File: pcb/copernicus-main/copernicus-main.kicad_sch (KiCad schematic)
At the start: 77 parts, among them J10 FAN_1, J11 FAN_2, J2 USB_C_14P, J3 BATT_IN, J4 CH_IN, J5 M1_PWR, J6 M2_PWR, J7 OUT_1, J8 OUT_2, J9 OUT_3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

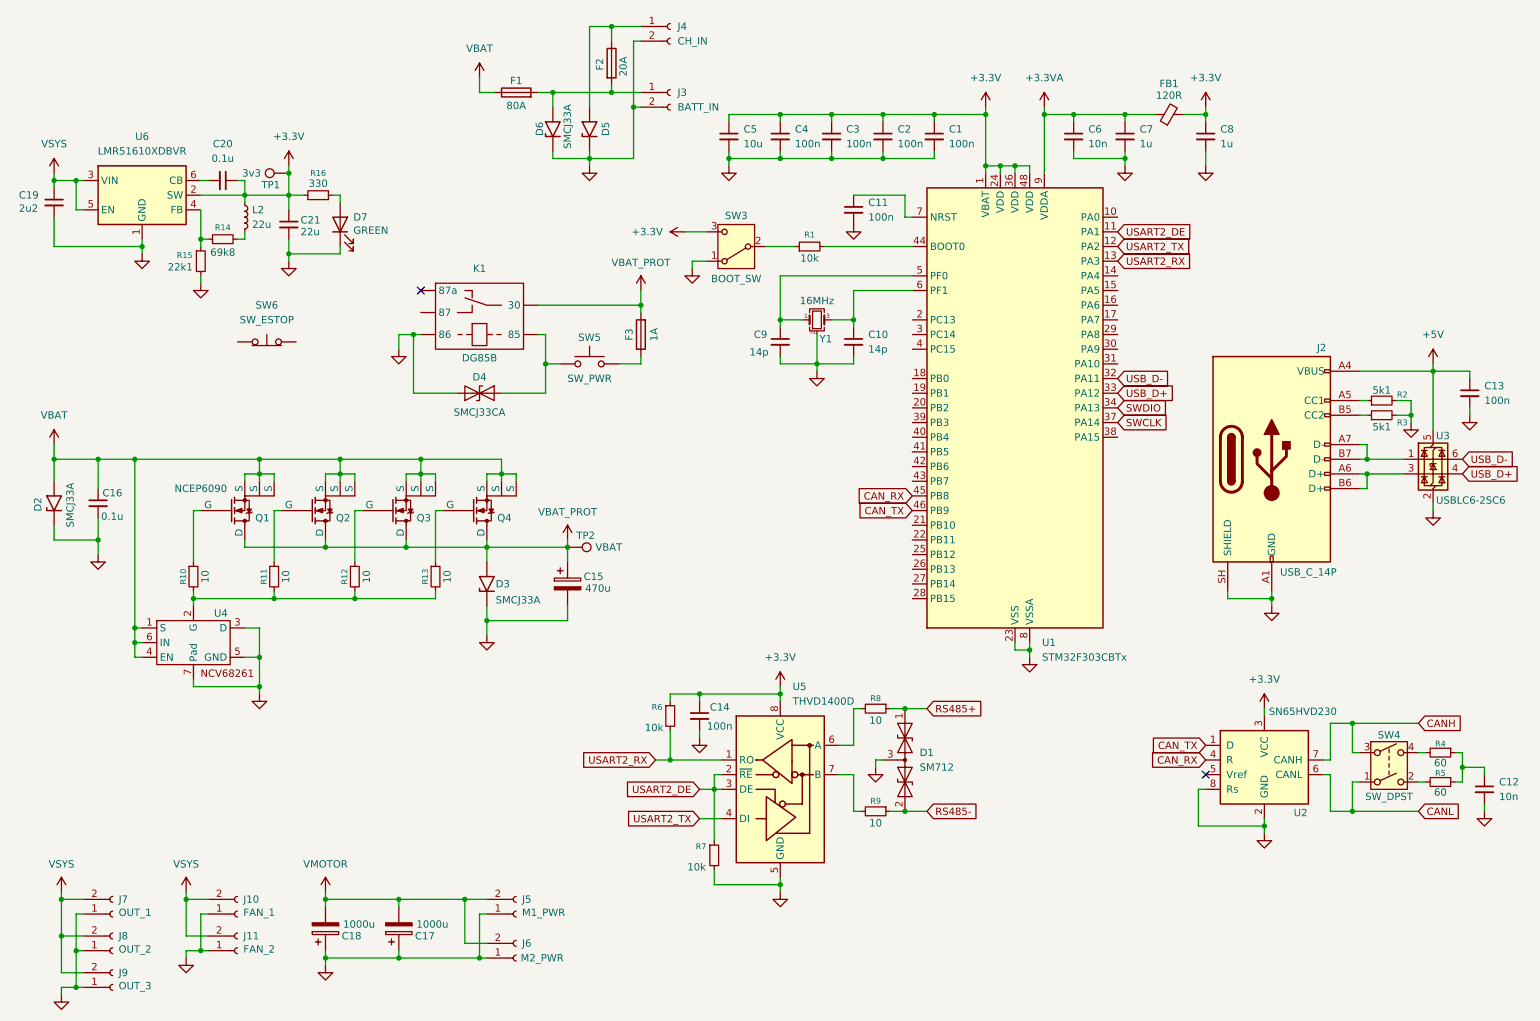
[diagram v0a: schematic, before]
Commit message: docs(pcb): added estop & mcu motor power control
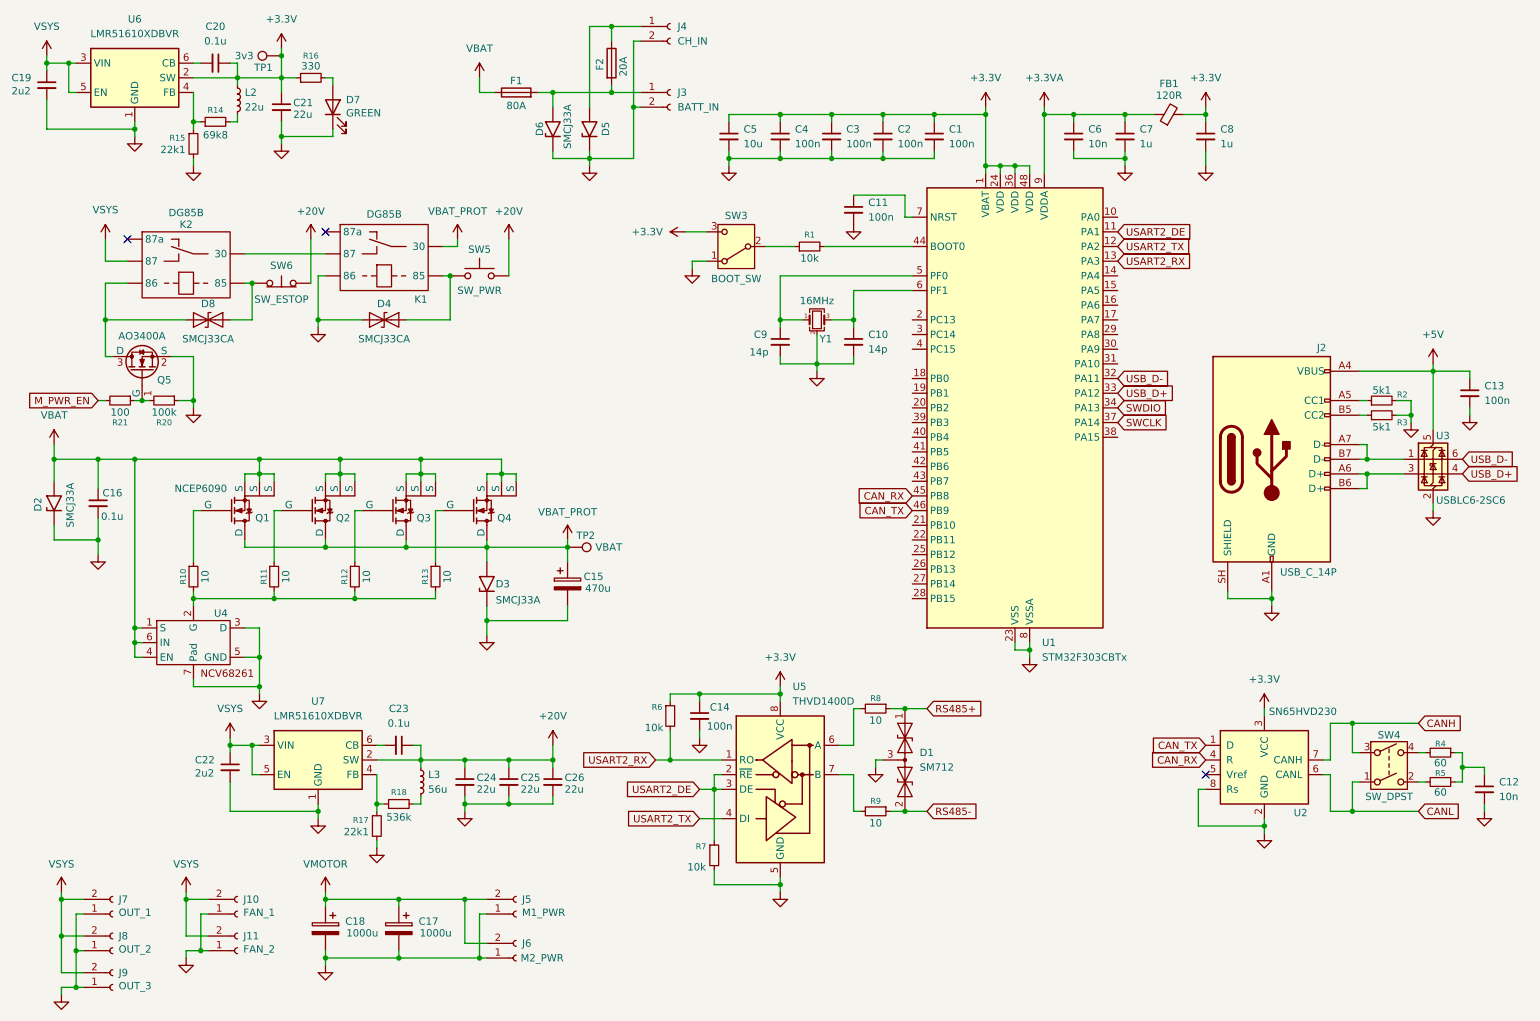
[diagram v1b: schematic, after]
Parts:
- removed F3: 1A, symbol Device:Fuse
- added C22: 2u2, symbol Device:C_Small
- added C23: 0.1u, symbol Device:C_Small
- added C24, C25, C26: 22u, symbol Device:C_Small
- added D8: SMCJ33CA, Diode_SMD:D_SOD-323, symbol component-addon:SMCJ33CA
- added K2: DG85B, symbol component-addon:DG85B
- added L3: 56u, symbol Device:L_Small
- added Q5: AO3400A, Package_TO_SOT_SMD:SOT-23, symbol Transistor_FET:AO3400A
- added R17: 22k1, symbol Device:R_Small
- added R18: 536k, symbol Device:R_Small
- added R20: 100k, symbol Device:R_Small
- added R21: 100, symbol Device:R_Small
- added U7: LMR51610XDBVR, Package_TO_SOT_SMD:SOT-23-6, symbol component-addon:LMR51610XDBVR
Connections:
- net GND: now also C17.2, C18.2, C22.2, C24.2, C25.2, C26.2, Q5.2 (S), R17.2, R20.1, U7.1 (GND); no longer C17.1, C18.1
- net VMOTOR: now also C17.1, C18.1; no longer C17.2, C18.2
- net VSYS: now also C22.1, K2. (85), U7.3 (VIN), U7.5 (EN)
- net +20V: now reaches SW5.2
- net +20V: now also SW6.2 (B), C23.1, C24.1, C25.1, C26.1, L3.1, U7.2 (SW)
- net at SW6.1 (A): now also D8.2 (A2), K2. (85)
- new net: C23.2, U7.6 (CB)
- new net: R17.1, R18.1, U7.4 (FB)
- new net: L3.2, R18.2
- new net: D8.1 (A1), K2. (85), Q5.3 (D)
- new net: K1. (85), K2. (85)
- new net: Q5.1 (G), R20.2, R21.1
- new net M_PWR_EN: R21.2
- no-connect marks 2 -> 3
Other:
- moved on the sheet: C19, C20, C21, D4, D7, K1, L2, R14, R15, R16, SW5, SW6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
